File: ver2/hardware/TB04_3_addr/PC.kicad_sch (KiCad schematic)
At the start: 16 parts, among them IC401 74HC161N, IC402 74HC161N, U401 74LS157, U402 74LS253, U403 74LS253, U404 74LS157, U405 74LS253, U406 74LS253

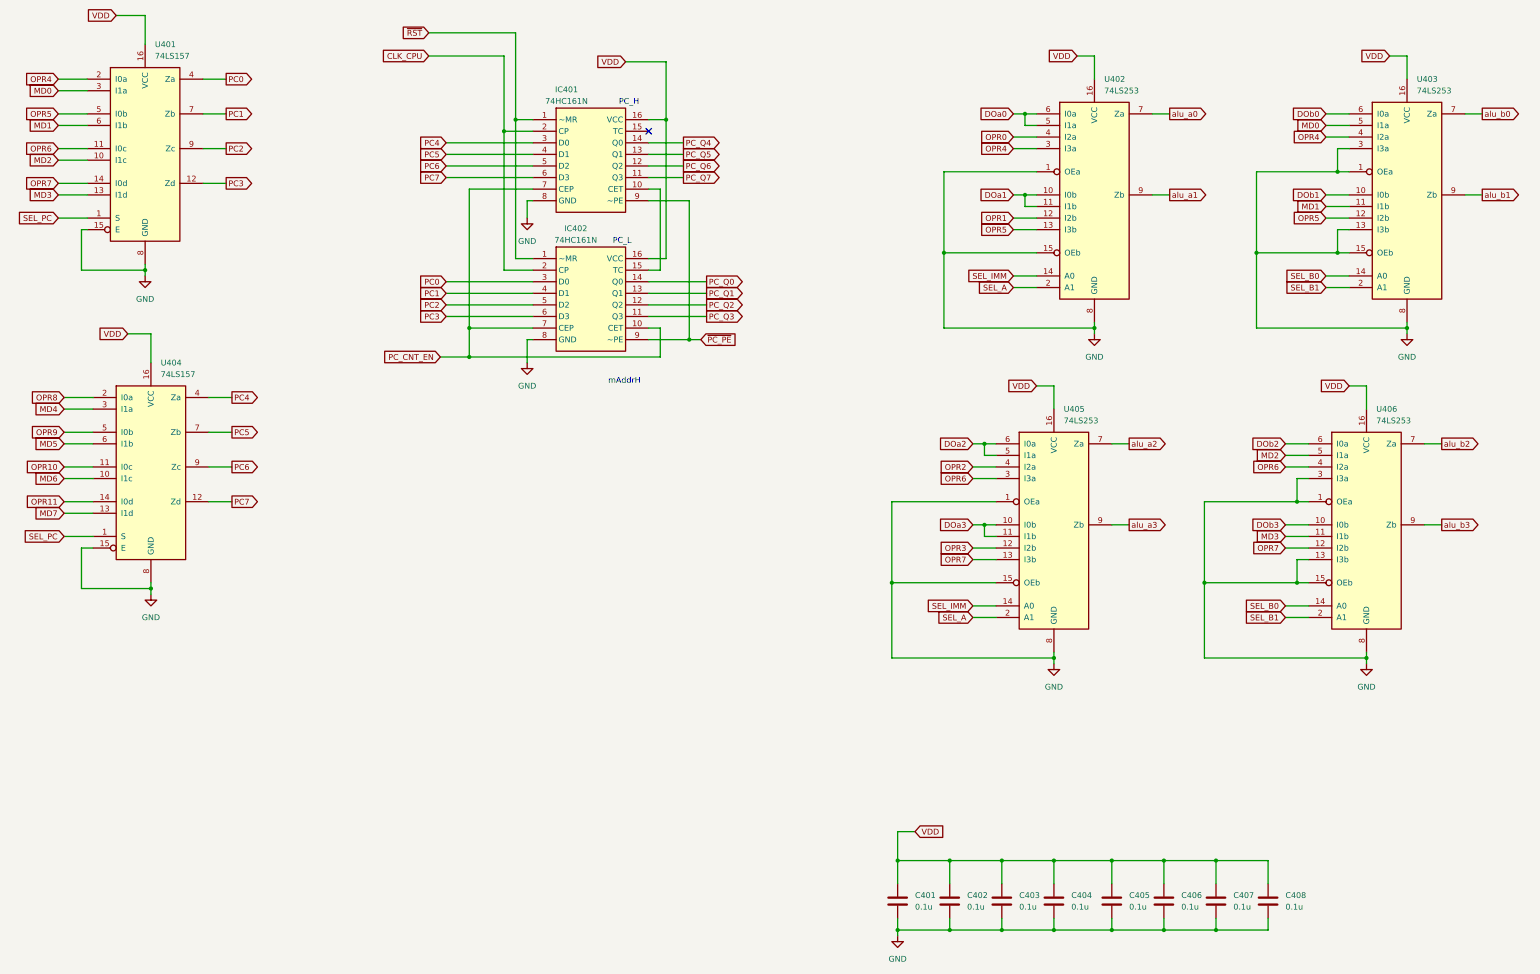
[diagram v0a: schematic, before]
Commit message: ver2: アドレス基板を分割し4枚すべて完了(要修正1件)
TB04_3_addr を分割。45部品・56信号すべてバスへ引き出し済み。
署名が変わったのは J101 のみ(USB-C→バスヘッダ)。
旧トップシート TB04addr8bit.kicad_sch も削除。

要修正: 3_addr の J103 で INPUT/OUTPUT のビット順が 4_io と逆
(pin25=INPUT0 になっている。正は pin25=INPUT3)

Co-Authored-By: Claude Opus 5 <noreply@anthropic.com>
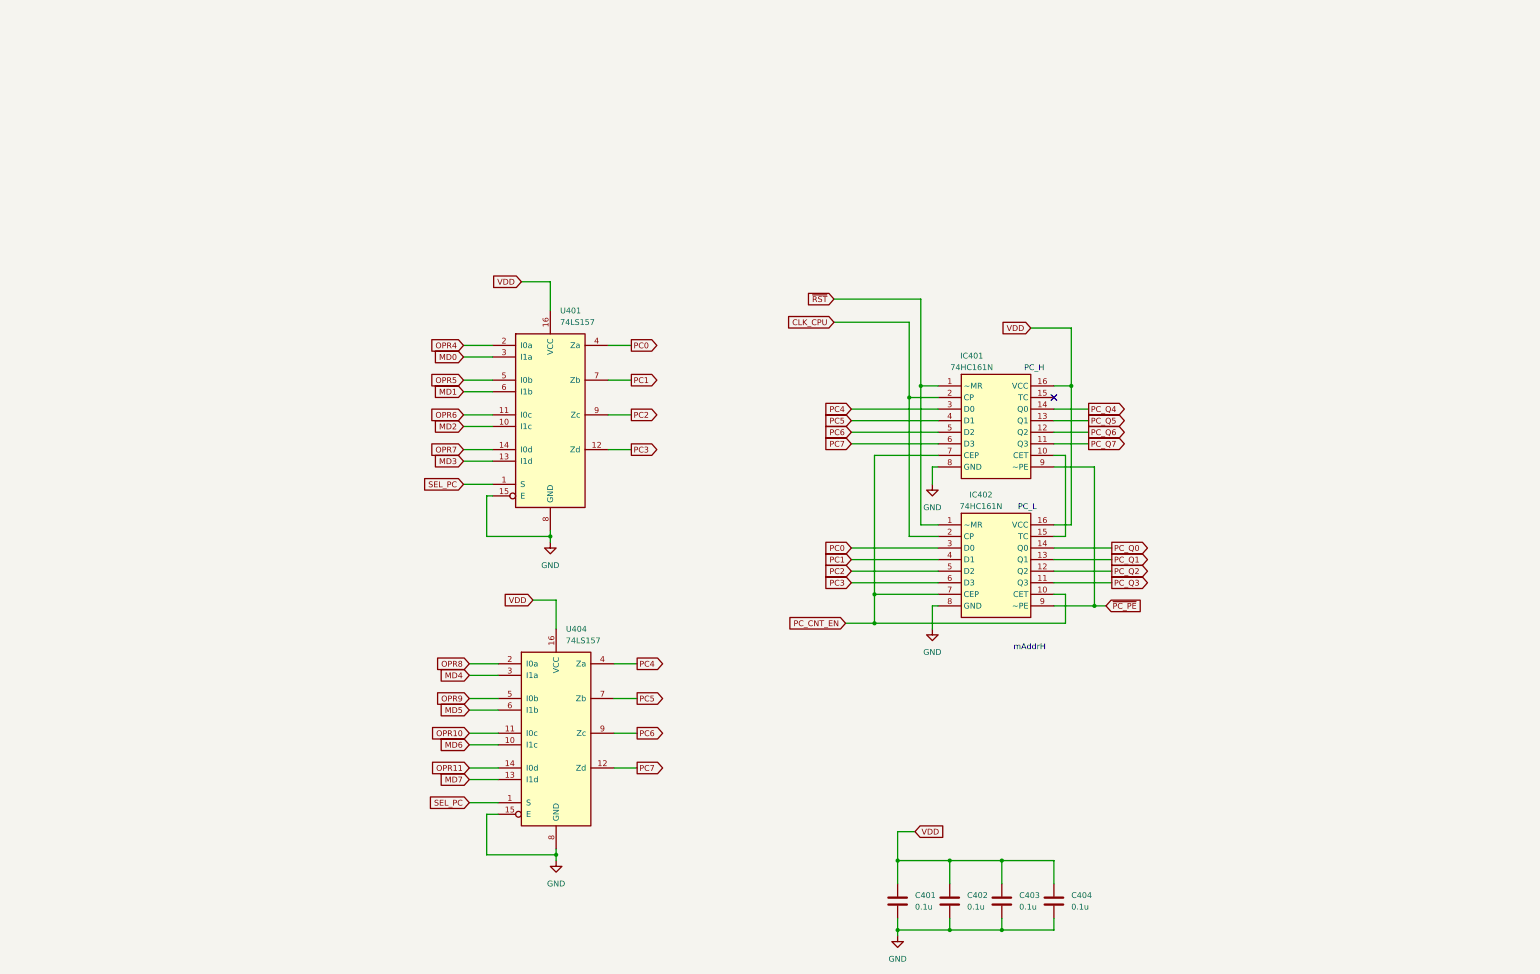
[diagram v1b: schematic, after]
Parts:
- removed C405, C406, C407, C408: 0.1u, symbol Device:C
- removed U402, U403, U405, U406: 74LS253, Package_DIP:DIP-16_W7.62mm_Socket, symbol 74xx:74LS253
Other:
- moved on the sheet: IC401, IC402, U401, U404
